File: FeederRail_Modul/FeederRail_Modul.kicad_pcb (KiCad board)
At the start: 2 copper layers, 125 x 24 mm, 50 parts, among them J101 Conn_02x07_Odd_Even, J102 Conn_02x07_Odd_Even, J103 Conn_02x07_Odd_Even, J104 Conn_02x07_Odd_Even, J105 Conn_02x07_Odd_Even

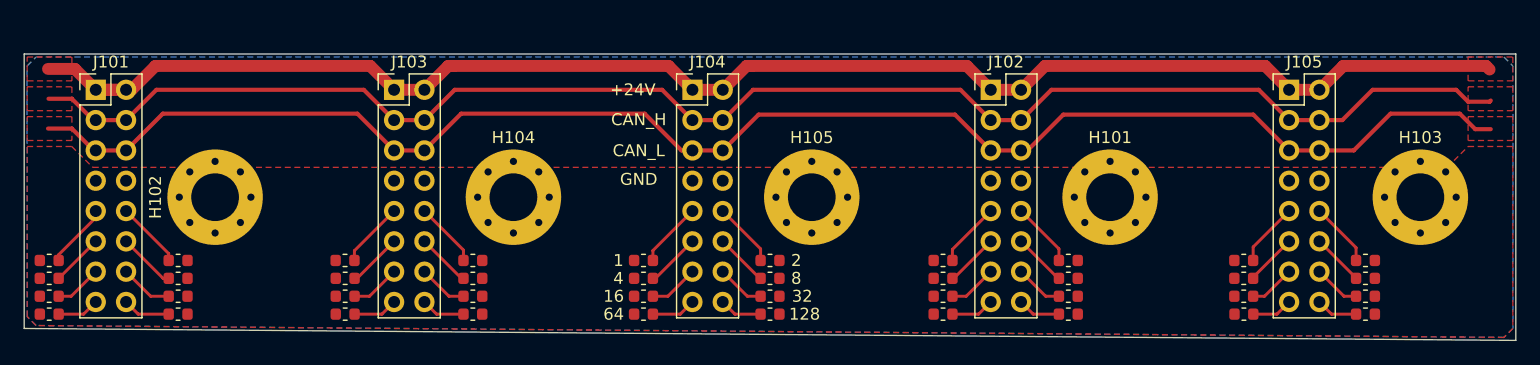
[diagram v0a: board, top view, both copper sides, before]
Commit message: Feeder Rail mit Step files geprüft. Connector am Feeder verschoeben. Halter für Lager muss angepasst werden.
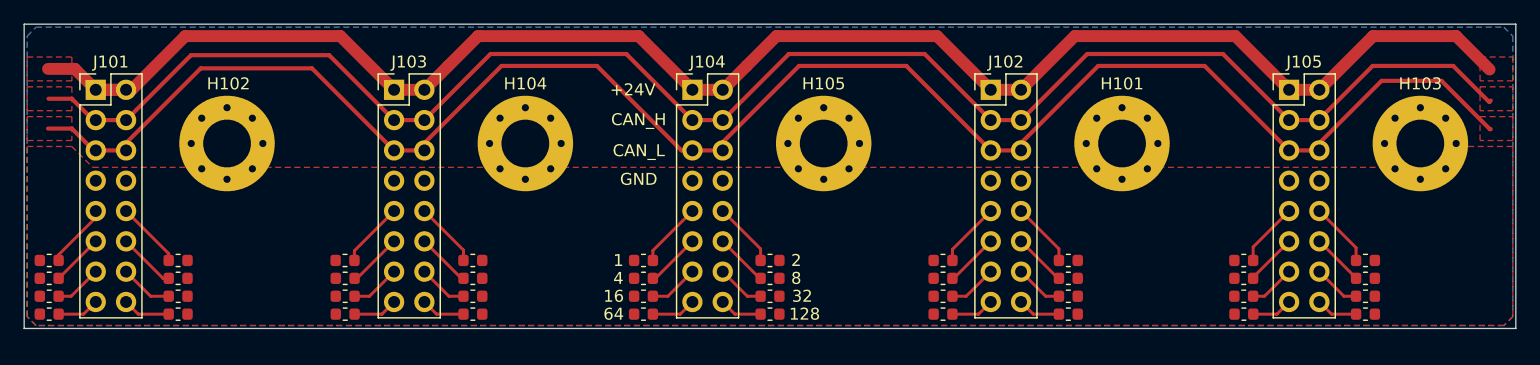
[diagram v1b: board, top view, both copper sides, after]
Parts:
- J101, J102, J103, J104, J105: footprint Connector_PinHeader_2.54mm:PinHeader_2x08_P2.54mm_Vertical -> ProjectFootprints:PinHeader_2x08_P2.54mm_Vertical
- moved H101 4.61 mm to (126.0, 34.5)
- moved H102 4.61 mm to (51.0, 34.5)
- moved H104 4.61 mm to (76.0, 34.5)
- moved H105 4.61 mm to (101.0, 34.5)
- moved H103 4.50 mm to (151.0, 34.5)
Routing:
- net /CAN1_L: track 133.5 -> 150.9 mm
- net /CAN1_H: track 131.5 -> 143.1 mm
- net +24V: track 131.6 -> 142.0 mm
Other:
- board size 125 x 24 mm -> 125 x 25.5 mm
